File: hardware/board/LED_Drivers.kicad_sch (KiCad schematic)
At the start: 10 parts

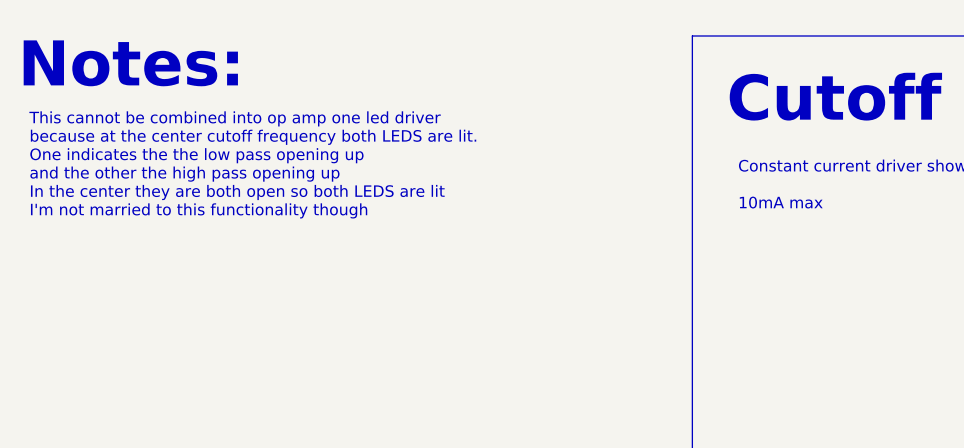
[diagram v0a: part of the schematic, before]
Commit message: Schematic getting closer to being finished
Schematic should be close to being ready to assign MPNs.
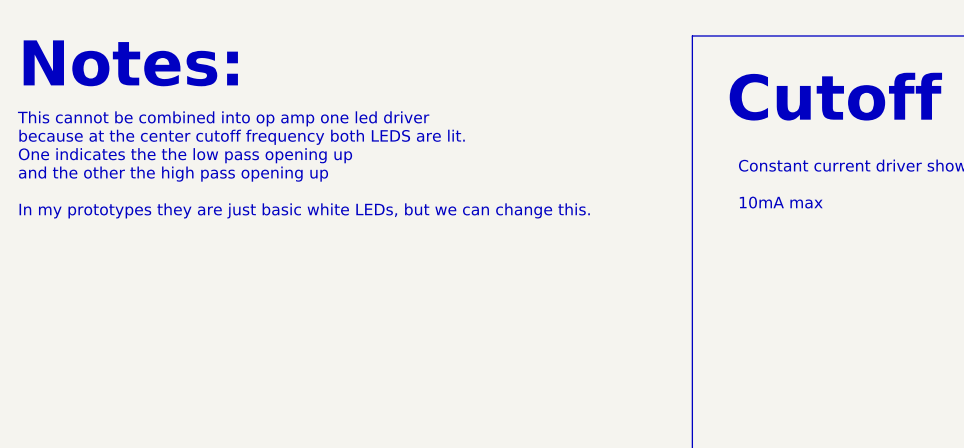
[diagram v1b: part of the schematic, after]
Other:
- note added: "This cannot be combined into op amp one led driver because at the center cutoff frequency both LEDS are lit. One indicates the the low pass opening up and the other the high pass opening up In my prototypes they are just basic white LEDs, but we can change this."
- note removed: "This cannot be combined into op amp one led driver because at the center cutoff frequency both LEDS are lit. One indicates the the low pass opening up and the other the high pass opening up In the center they are both open so both LEDS are lit I'm not married to this functionality though"
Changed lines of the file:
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@@
     (effects (font (size 5 5) (thickness 0.508) bold) (justify left bottom))
   )
-  (text "This cannot be combined into op amp one led driver\nbecause at the center cutoff frequency both LEDS are lit.\nOne indicates the the low pass opening up\nand the other the high pass opening up\nIn the center they are both open so both LEDS are lit\nI'm not married to this functionality though"
-    (at 17.78 41.91 0)
+  (text "This cannot be combined into op amp one led driver\nbecause at the center cutoff frequency both LEDS are lit.\nOne indicates the the low pass opening up\nand the other the high pass opening up\n\nIn my prototypes they are just basic white LEDs, but we can change this."
+    (at 16.51 41.91 0)
     (effects (font (size 1.27 1.27)) (justify left bottom))
   )

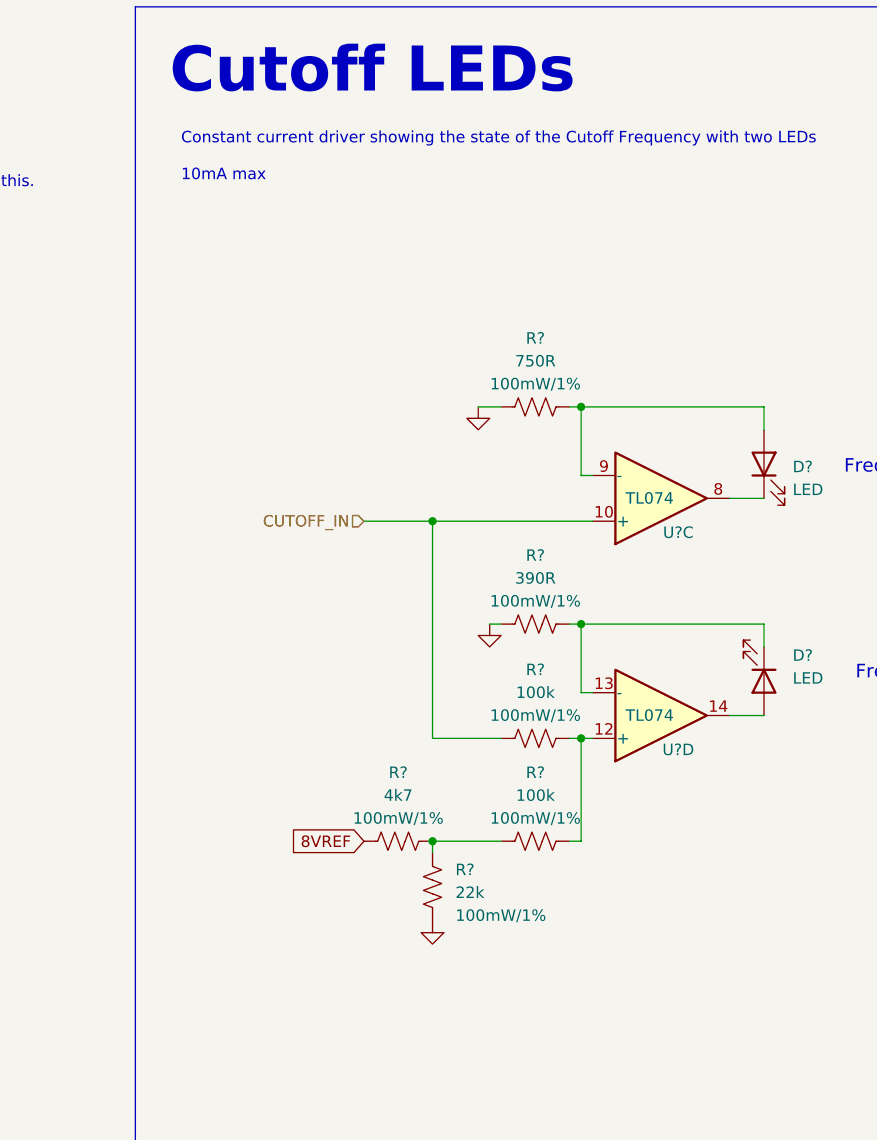
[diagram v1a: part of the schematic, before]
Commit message: BOM Consolidation
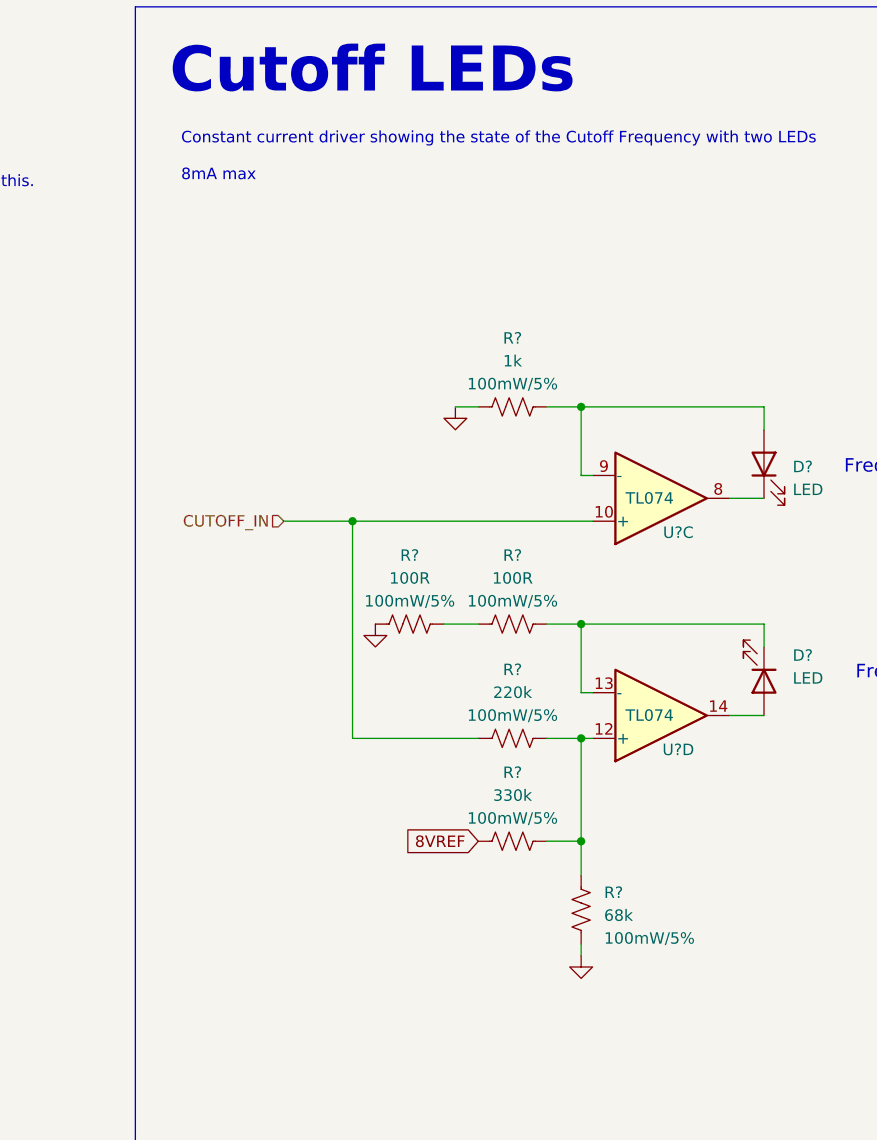
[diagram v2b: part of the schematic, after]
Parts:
- removed R?: 4k7, winterbloom:R_0603_HandSolder, symbol Device:R_US
- removed R?: 390R, winterbloom:R_0603_HandSolder, symbol Device:R_US
- removed R?: 22k, winterbloom:R_0603_HandSolder, symbol Device:R_US
- added R?: 68k, winterbloom:R_0603_HandSolder, symbol Device:R_US
- added R? (x2): 100R, winterbloom:R_0603_HandSolder, symbol Device:R_US
- R?: value 100k -> 330k; Rating 100mW/1% -> 100mW/5%
- R?: value 100k -> 220k; Rating 100mW/1% -> 100mW/5%
- R?: value 750R -> 1k; Rating 100mW/1% -> 100mW/5%
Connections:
- net 8VREF: now also R?.2
- net GND: now also R?.2, R?.2
- net at R?.1, R?.1, U?.12 (+): now also R?.1
- net at D?.1 (K), U?.13 (-): now also R?.1
- new net: R?.1, R?.2
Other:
- note added: "Constant current driver showing the state of the Cutoff Frequency with two LEDs 8mA max"
- note removed: "Constant current driver showing the state of the Cutoff Frequency with two LEDs 10mA max"
- moved on the sheet: R?

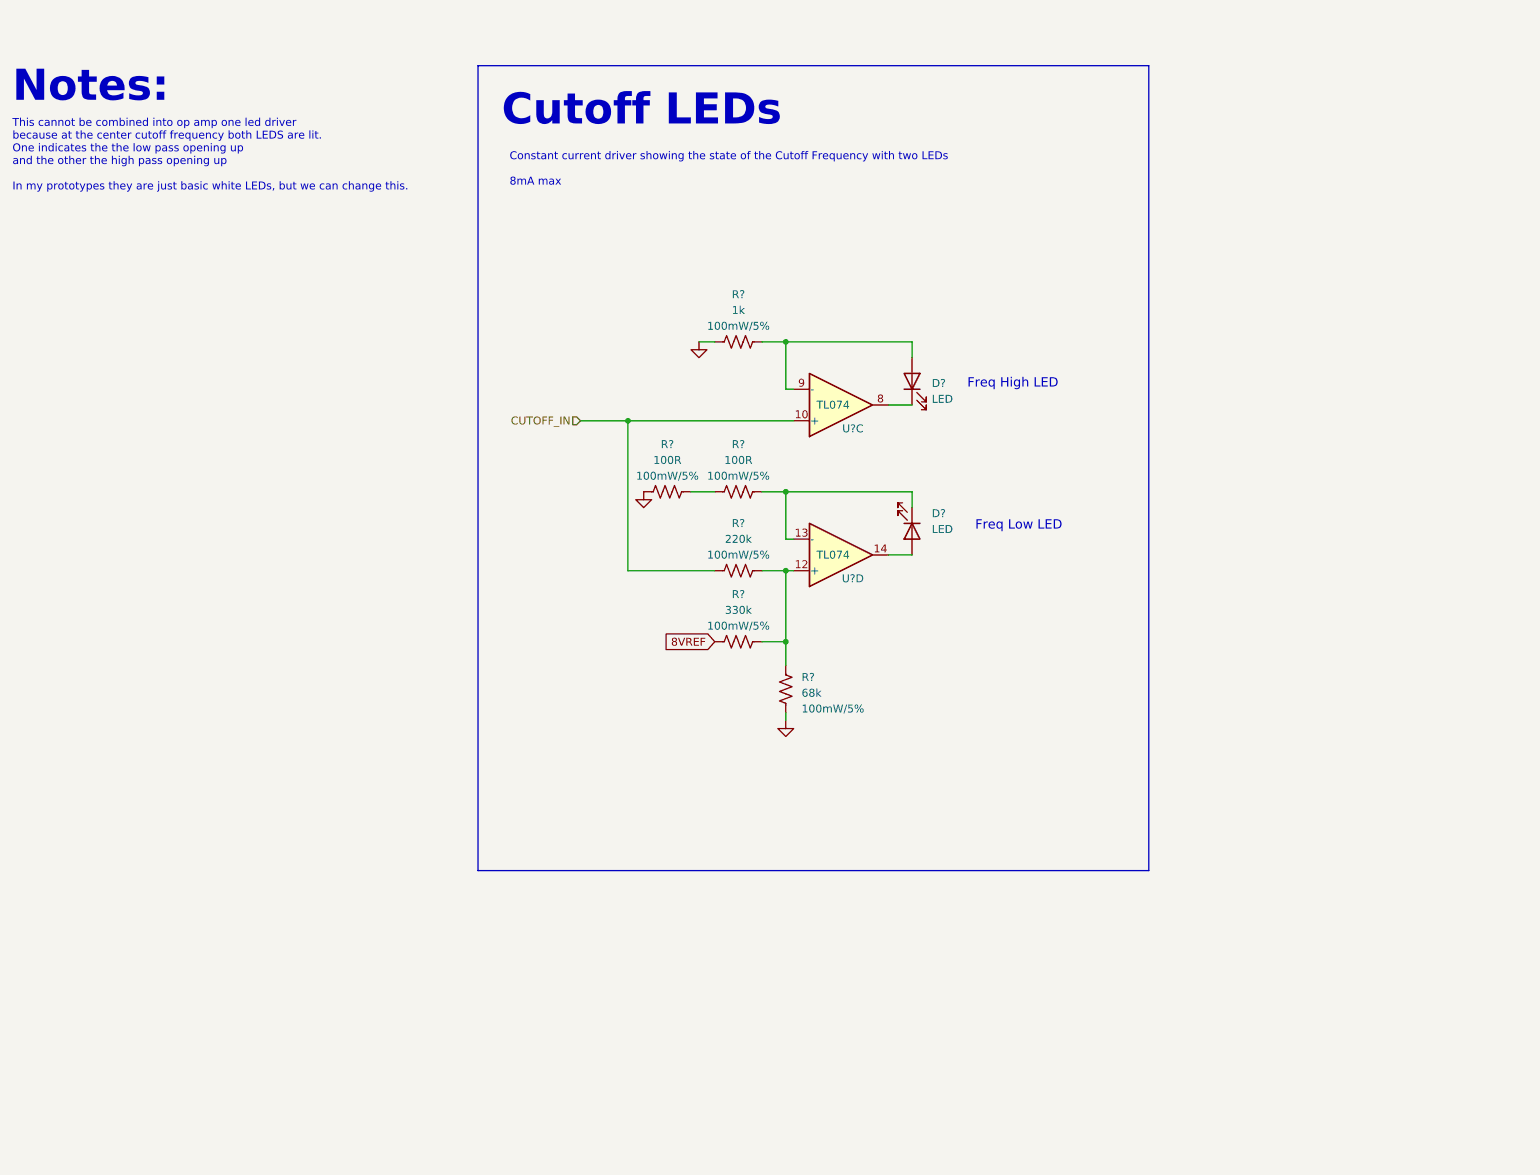
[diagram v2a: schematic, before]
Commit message: Updates for LED Drivers
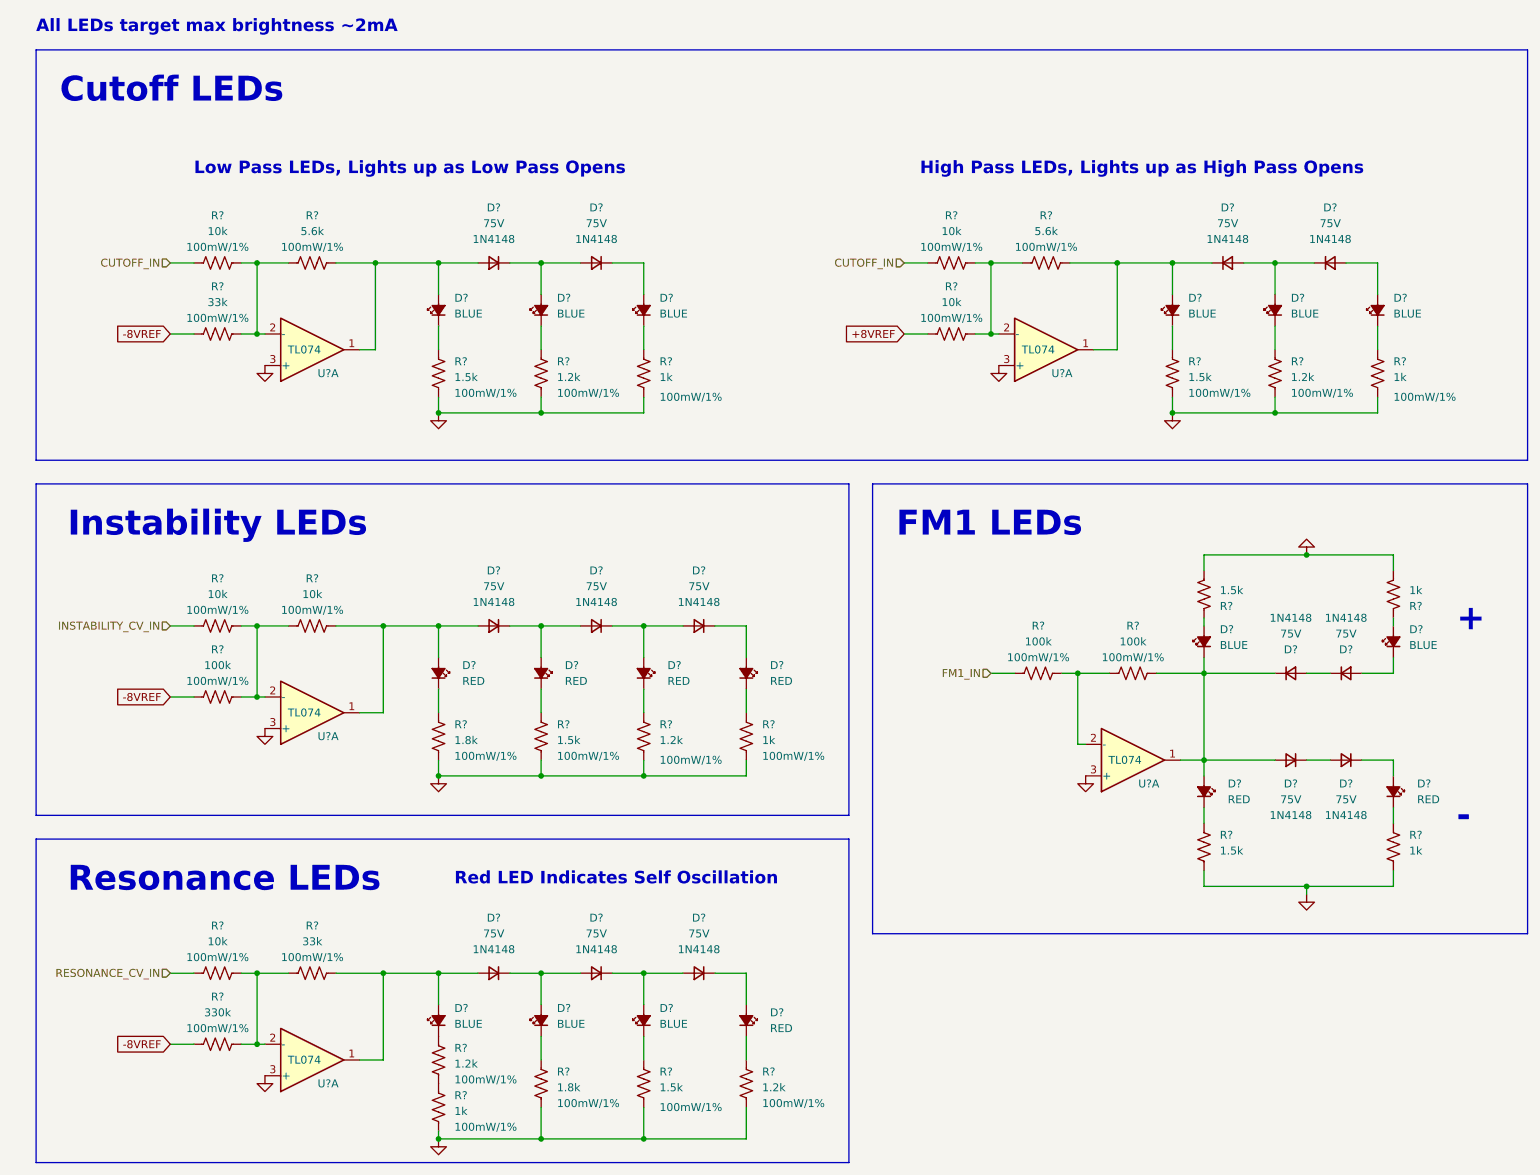
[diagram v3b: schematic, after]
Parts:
- removed D? (x2): LED, LED_SMD:LED_0805_2012Metric, symbol Device:LED
- removed R?: 330k, winterbloom:R_0603_HandSolder, symbol Device:R_US
- removed R?: 68k, winterbloom:R_0603_HandSolder, symbol Device:R_US
- removed R? (x2): 100R, winterbloom:R_0603_HandSolder, symbol Device:R_US
- removed R?: 220k, winterbloom:R_0603_HandSolder, symbol Device:R_US
- removed R?: 1k, winterbloom:R_0603_HandSolder, symbol Device:R_US
- removed U? (x2): TL074, Package_SO:TSSOP-14_4.4x5mm_P0.65mm, symbol winterbloom:TL074
- added D? (x14): 75V, Diode_SMD:D_SOD-123, symbol Device:D_Small
- added D? (x7): RED, winterbloom:LED_0805_Kingbright_APT2012, symbol Device:LED_Small_Filled
- added D? (x11): BLUE, winterbloom:LED_0805_Kingbright_APT2012, symbol Device:LED_Small_Filled
- added R? (x2): 5.6k, winterbloom:R_0603_HandSolder, symbol Device:R_US
- added R? (x6): 1.5k, winterbloom:R_0603_HandSolder, symbol Device:R_US
- added R? (x6): 1k, winterbloom:R_0603_HandSolder, symbol Device:R_US
- added R? (x6): 10k, winterbloom:R_0603_HandSolder, symbol Device:R_US
- added R? (x2): 33k, winterbloom:R_0603_HandSolder, symbol Device:R_US
- added R? (x5): 1.2k, winterbloom:R_0603_HandSolder, symbol Device:R_US
- added R? (x3): 100k, winterbloom:R_0603_HandSolder, symbol Device:R_US
- added R? (x2): 1.8k, winterbloom:R_0603_HandSolder, symbol Device:R_US
- added R?: 330k, winterbloom:R_0603_HandSolder, symbol Device:R_US
- added U? (x5): TL074, Package_SO:TSSOP-14_4.4x5mm_P0.65mm, symbol winterbloom:TL074
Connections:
- net CUTOFF_IN: now also R?.2, R?.2
- net GND: now also R?.2, R?.2, R?.2, R?.2, R?.2, R?.2, R?.2, R?.2, R?.2, R?.2, R?.2, R?.2, R?.2, R?.2, R?.2, R?.2, R?.2, R?.2, U?.3 (+), U?.3 (+), U?.3 (+), U?.3 (+), U?.3 (+)
- new net: D?.1 (K), D?.2 (A) (x7)
- new net: D?.1 (K), D?.1 (K), D?.2 (A), D?.2 (A), R?.1, U?.1
- new net: D?.1 (K), R?.1 (x16)
- new net: D?.1 (K), D?.2 (A), R?.1, U?.1
- new net: R?.1, R?.1, R?.2, U?.2 (-) (x4)
- new net: D?.2 (A), R?.1 (x2)
- new net: D?.1 (K), D?.2 (A), D?.2 (A) (x6)
- new net: D?.2 (A), D?.2 (A), R?.1, U?.1 (x3)
- new net: R?.1, R?.2
- new net: R?.1, R?.2, U?.2 (-)
- new net: D?.2 (A), D?.2 (A)
- new net +8VREF: R?.2
- new net -8VREF: R?.2, R?.2, R?.2
- new net FM1_IN: R?.2
- new net INSTABILITY_CV_IN: R?.2
- new net RESONANCE_CV_IN: R?.2
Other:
- note added: "+"
- note added: "-"
- note added: "All LEDs target max brightness ~2mA"
- note added: "FM1 LEDs"
- note added: "High Pass LEDs, Lights up as High Pass Opens"
- note added: "Instability LEDs"
- note added: "Low Pass LEDs, Lights up as Low Pass Opens"
- note added: "Red LED Indicates Self Oscillation"
- note added: "Resonance LEDs"
- note removed: "Constant current driver showing the state of the Cutoff Frequency with two LEDs 8mA max"
- note removed: "Freq High LED"
- note removed: "Freq Low LED"
- note removed: "Notes:"
- note removed: "This cannot be combined into op amp one led driver because at the center cutoff frequency both LEDS are lit. One indicates the the low pass opening up and the other the high pass opening up In my prototypes they are just basic white LEDs, but we can change this."

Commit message: Few cleanups for LED drivers
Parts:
- removed R?: 1k, winterbloom:R_0603_HandSolder, symbol Device:R_US
- R?: value 1.2k -> 1.8k
- R?: value 1.5k -> 1.2k
- R?: value 1.2k -> 1k
- R?: value 1.8k -> 1.5k
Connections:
- net GND: now also R?.2
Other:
- moved on the sheet: D?, R?, U?A

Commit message: hardware: update schematic with footprints and preliminary MPNs
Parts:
- D? (x14): value 75V -> BAS315; footprint Diode_SMD:D_SOD-123 -> winterbloom:D_SOD-323; LCSC C81598 -> (none); MPN 1N4148W -> BAS316,115; Manufacturer ST(Semtech) -> (none); Notes (none) -> Voltage drop diode; Rating 1N4148 -> 1Vf @ 100mA
- D? (x7): MPN (none) -> APT2012SURCK; mpn APT2012SURCK -> (none); smd kit 1 -> (none)
- D? (x11): MPN (none) -> APT2012VBC/D; mpn APT2012VBC/D -> (none); smd kit 1 -> (none)
- R? (x2): value 5.6k -> 5k6; smd kit 1 -> (none)
- R? (x6): value 1.5k -> 1k5; smd kit 1 -> (none)
- R? (x24): smd kit 1 -> (none)
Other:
- title: Diode Ladder Filter -> Neptune

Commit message: Very first component layout.
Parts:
- removed U?: TL074, Package_SO:TSSOP-14_4.4x5mm_P0.65mm, symbol winterbloom:TL074
- added U?: TL074, Package_SO:TSSOP-14_4.4x5mm_P0.65mm, symbol winterbloom:TL074
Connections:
- net GND: now also U?.10 (+)
- net at D?.1 (K), D?.1 (K), D?.2 (A)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: now also U?.1; no longer U?.1
- net at D?.1 (K), D?.2 (A), R?.1: now also U?.1; no longer U?.1
- net at R?.1, R?.1, R?.2: now also U?.2 (-); no longer U?.2 (-)
- net at R?.1, R?.1, R?.2: no longer U?.2 (-)
- net at D?.2 (A), D?.2 (A), R?.1: now also U?.1; no longer U?.1
- net at R?.1, R?.1, R?.2: now also U?.9 (-)
- net at R?.1, R?.2: now also U?.2 (-); no longer U?.2 (-)
- net at D?.2 (A), D?.2 (A), R?.1: now also U?.8
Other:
- moved on the sheet: U?A
